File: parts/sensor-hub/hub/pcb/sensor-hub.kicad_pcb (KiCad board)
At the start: 2 copper layers, 85.7 x 47 mm, 13 parts, among them J1 MPT1584 buck, J2 PWR IN, SW2 SW_SPDT, U1 ESP32 Wemos D1 Mini

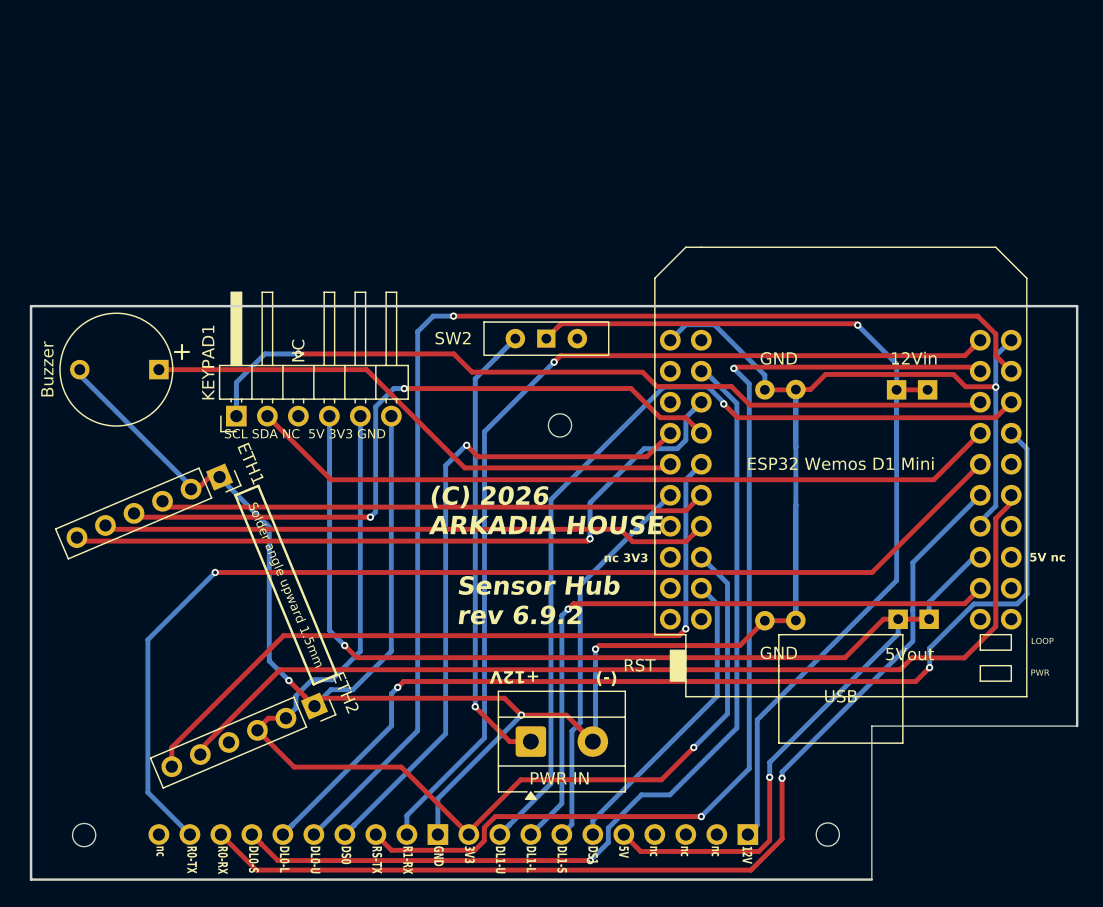
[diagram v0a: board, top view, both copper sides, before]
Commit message: move ETH to back, change whole layout, prep for addl DC buck and 24V input.
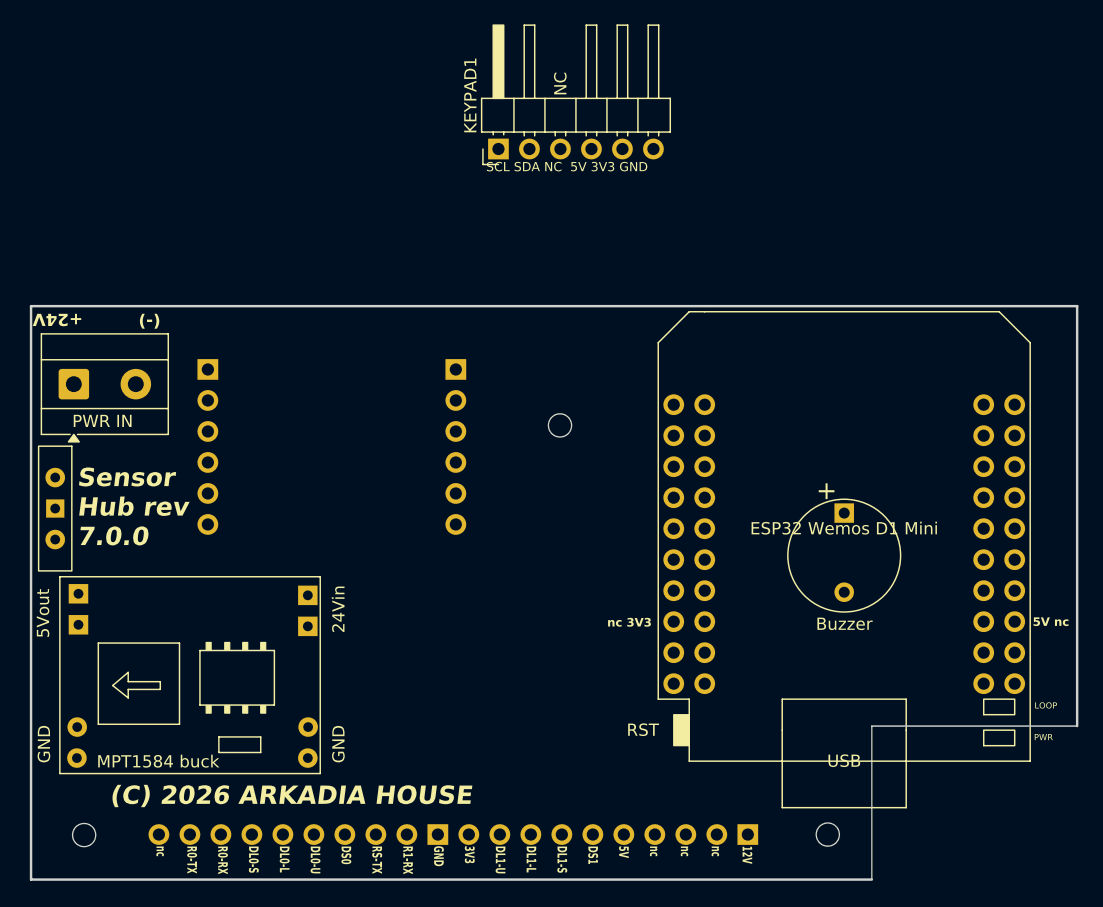
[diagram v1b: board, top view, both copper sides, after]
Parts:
- ETH1, ETH2: moved to B.Cu
- J1: moved to F.Cu
- moved BZ1 59.1 mm to (166.8, 71.5), turned to 0 degrees
- moved J1 55.6 mm to (112.6, 83.8), turned to 180 degrees
- moved J2 47.5 mm to (103.6, 59.4)
- moved SW2 42.6 mm to (102.1, 69.6), turned to -90 degrees
- moved KEYPAD1 30.7 mm to (138.4, 40.1)
- moved ETH2 28.9 mm to (114.6, 58.2), turned to 180 degrees
- moved ETH1 21.3 mm to (134.9, 58.2), turned to 180 degrees
- moved U1 5.29 mm to (166.8, 72.5)
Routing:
- net GND: track 208.5 -> 0.00 mm, vias 4 -> 0
- net /5V: track 110.9 -> 0.00 mm, vias 2 -> 0
- net /DL0_UNLOCK: track 96.8 -> 0.00 mm, vias 1 -> 0
- net /R0_TXD_TO_RXD: track 91.6 -> 0.00 mm, vias 1 -> 0
- net /3V3: track 90.7 -> 0.00 mm, vias 1 -> 0
- net /R1_TXD_TO_RXD: track 87.7 -> 0.00 mm, vias 2 -> 0
- net /DL0_LOCK: track 86.5 -> 0.00 mm, vias 2 -> 0
- net /12V: track 83.2 -> 0.00 mm, vias 1 -> 0
- net /R0_RXD_TO_TXD: track 83.2 -> 0.00 mm, vias 1 -> 0
- net /R1_RXD_TO_TXD: track 80.3 -> 0.00 mm, vias 1 -> 0
- net Net-(ETH2-RST): track 80.0 -> 0.00 mm
- net /DL0_SENSE: track 77.3 -> 0.00 mm, vias 1 -> 0
- net /DL1_UNLOCK: track 73.5 -> 0.00 mm, vias 1 -> 0
- net /SCL: track 67.4 -> 0.00 mm, vias 1 -> 0
- net /SDA: track 62.2 -> 0.00 mm
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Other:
- board text added: "RJ45 this side"
- board text added: "Sensor Hub rev 7.0.0"
- board text removed: "GND 3V3 3V3 nc ETH-RS MISO"
- board text removed: "GND GND MOSI SCK CS INT"
- board text removed: "Sensor Hub rev 6.9.2"
- board text removed: "Solder angle upward 1.5mm"

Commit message: hub 7.0
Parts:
- added BUCK2: MPT1584 buck, local_project:SRT_MPT1584EN_Module, F.Cu at (138.6, 84.0)
- BUCK1: renamed from J1; footprint sensor hub.04:SRT_MPT1584EN_Module -> local_project:SRT_MPT1584EN_Module
- KEYPAD1: value Conn_01x06 -> Conn_01x05; footprint Connector_PinHeader_2.54mm:PinHeader_1x06_P2.54mm_Horizontal -> Connector_PinHeader_2.54mm:PinHeader_1x05_P2.54mm_Horizontal
- U1: footprint sensor hub.04:esp32-wemos-d1-mini -> local_project:esp32-wemos-d1-mini
- moved KEYPAD1 18.9 mm to (139.1, 59.0)
- moved BUCK1 0.76 mm to (111.9, 83.8)
- renumbered J2 to PWR1, SW2 to SW1
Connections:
- net +12V renamed +24V
- BUCK1 pad 1: /12V -> Net-(BUCK1-24Vin)
- KEYPAD1 pad 3: unconnected-(KEYPAD1-NC-Pad3) -> GND
- MCU-TO-CBL-A1 pad 3: unconnected-(MCU-TO-CBL-A1-Pin_3-Pad3) -> Net-(BUCK1-24Vin)
- SW1 pad 1: /12V -> Net-(BUCK1-24Vin)
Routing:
- net GND: track 0.00 -> 203.4 mm
- net /5V: track 0.00 -> 120.0 mm, vias 0 -> 2
- net /3V3: track 0.00 -> 107.3 mm, vias 0 -> 1
- net /R0_TXD_TO_RXD: track 0.00 -> 96.7 mm, vias 0 -> 5
- net /DL0_UNLOCK: track 0.00 -> 95.6 mm, vias 0 -> 1
- net /R1_RXD_TO_TXD: track 0.00 -> 88.8 mm, vias 0 -> 1
- net /DL0_LOCK: track 0.00 -> 82.0 mm, vias 0 -> 2
- net /R1_TXD_TO_RXD: track 0.00 -> 79.6 mm, vias 0 -> 1
- net /R0_RXD_TO_TXD: track 0.00 -> 78.8 mm, vias 0 -> 1
- net Net-(BUCK1-24Vin): track 0.00 -> 78.3 mm
- net Net-(ETH2-RST): track 0.00 -> 73.1 mm
- net /DL1_UNLOCK: track 0.00 -> 67.8 mm, vias 0 -> 2
- net /DL0_SENSE: track 0.00 -> 67.0 mm, vias 0 -> 1
- net /MOSI: track 0.00 -> 58.9 mm, vias 0 -> 3
- net /DS0_SENSE: track 0.00 -> 52.8 mm, vias 0 -> 1
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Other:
- board text added: "12V 12V"
- board text added: "12V nc 24V nc 5V DS1 DL1-S DL1-L DL1-U 3V3 GND R1-RX RS-TX DS0 DL0-U DL0-L DL0-S R0-RX R0-TX nc"
- board text added: "24V 24V"
- board text added: "5V 5V"
- board text added: "SCL SDA GND 5V 3V3"
- board text removed: "12V nc nc nc 5V DS1 DL1-S DL1-L DL1-U 3V3 GND R1-RX RS-TX DS0 DL0-U DL0-L DL0-S R0-RX R0-TX nc"
- board text removed: "SCL SDA NC 5V 3V3 GND"
